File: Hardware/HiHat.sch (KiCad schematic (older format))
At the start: 34 parts, among them J1 CH trig in, J2 OH trig in, J3 IDC power connector, Q1 BC549, Q2 BC549, Q3 BC549, Q4 BC549

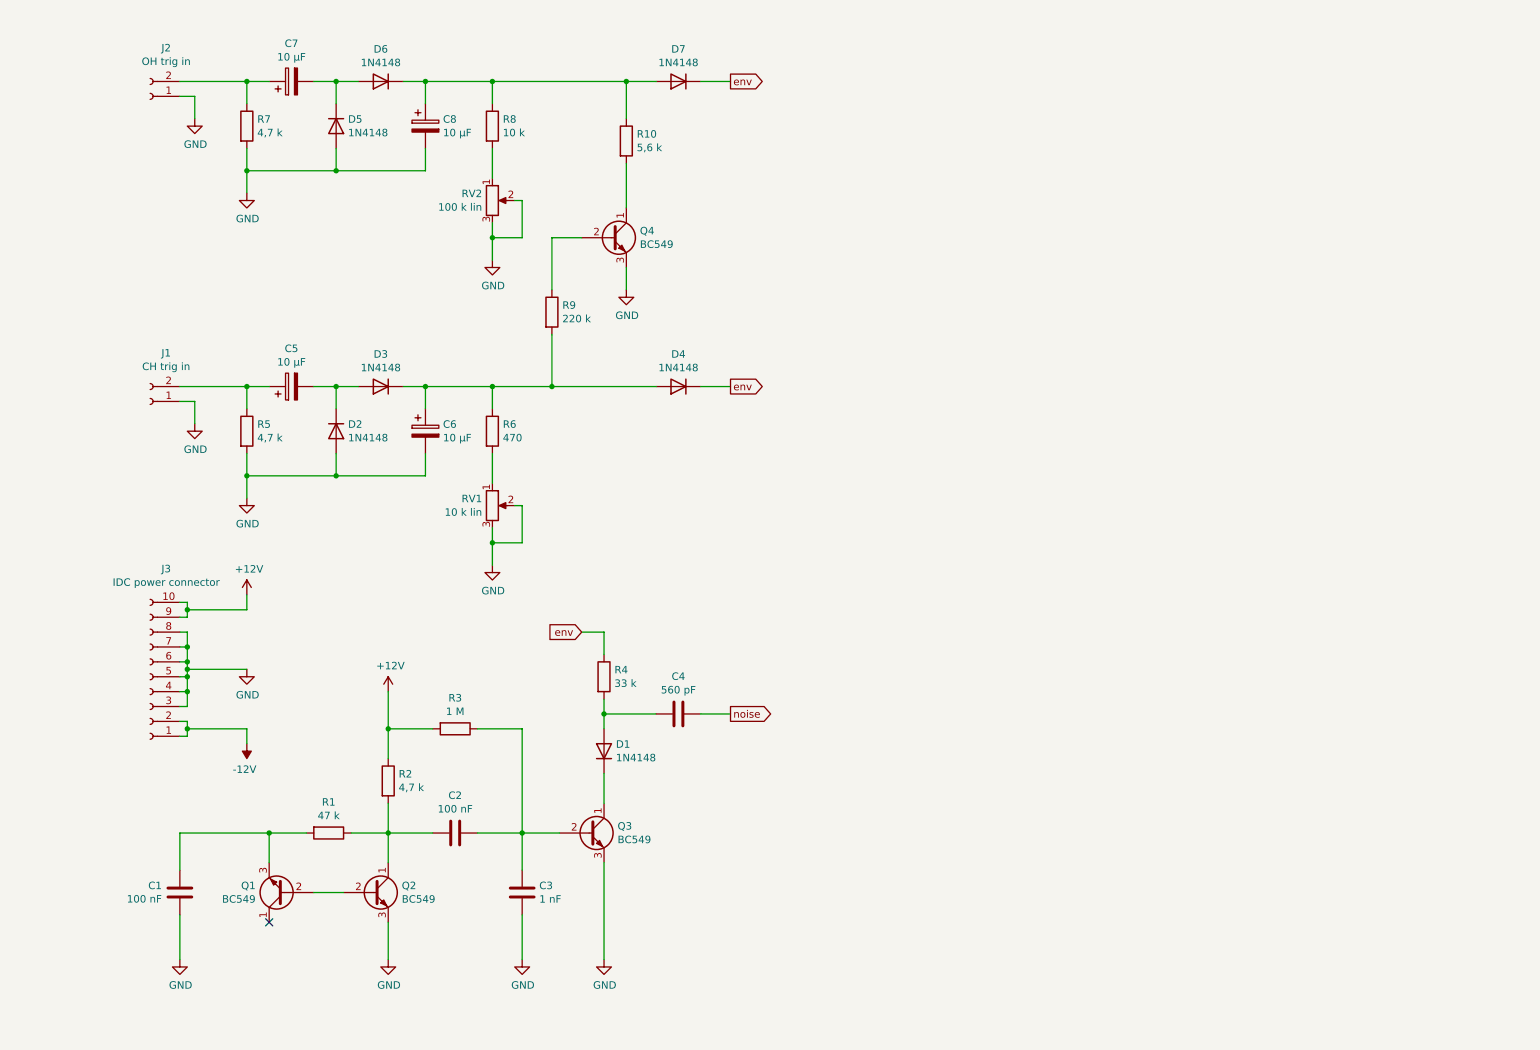
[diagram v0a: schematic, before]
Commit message: Added input conditioners and output buffer
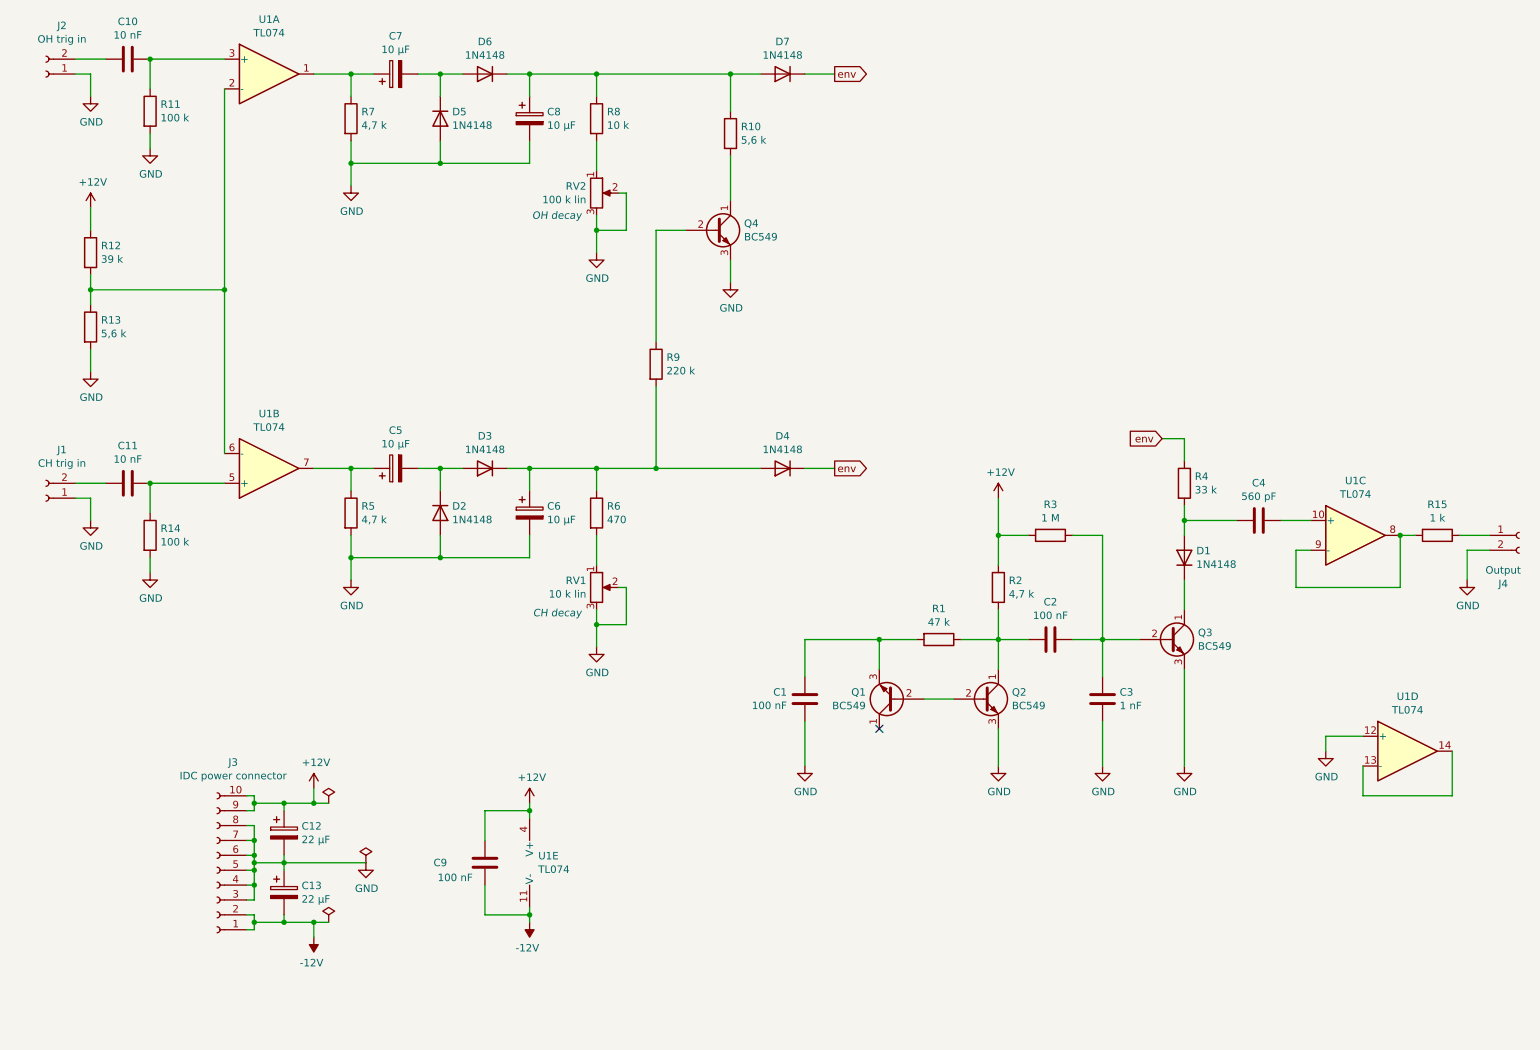
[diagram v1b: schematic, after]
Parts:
- added C10, C11: 10 nF, Capacitor_THT:C_Rect_L7.2mm_W5.5mm_P5.00mm_FKS2_FKP2_MKS2_MKP2, symbol Device:C
- added C12, C13: 22 µF, Capacitor_THT:CP_Radial_D6.3mm_P2.50mm, symbol Device:CP
- added C9: 100 nF, Capacitor_THT:C_Rect_L7.2mm_W5.5mm_P5.00mm_FKS2_FKP2_MKS2_MKP2, symbol Device:C
- added J4: Output, Connector_PinHeader_2.54mm:PinHeader_1x02_P2.54mm_Vertical, symbol Connector:Conn_01x02_Female
- added R11, R14: 100 k, Resistor_THT:R_Axial_DIN0207_L6.3mm_D2.5mm_P10.16mm_Horizontal, symbol Device:R
- added R12: 39 k, Resistor_THT:R_Axial_DIN0207_L6.3mm_D2.5mm_P10.16mm_Horizontal, symbol Device:R
- added R13: 5,6 k, Resistor_THT:R_Axial_DIN0207_L6.3mm_D2.5mm_P10.16mm_Horizontal, symbol Device:R
- added R15: 1 k, Resistor_THT:R_Axial_DIN0207_L6.3mm_D2.5mm_P10.16mm_Horizontal, symbol Device:R
- added U1: TL074, symbol Amplifier_Operational:TL074
- RV1: Label (none) -> CH decay
- RV2: Label (none) -> OH decay
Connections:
- net +12V: now also C12.1, C9.1, R12.1, U1.4 (V+)
- net -12V: now also C13.2, C9.2, U1.11 (V-)
- net GND: now also C12.2, C13.1, J4.2 (Pin_2), R11.2, R13.2, R14.2, U1.12 (+)
- net at C5.1, R5.1: now also U1.7; no longer J1.2 (Pin_2)
- net at C7.1, R7.1: now also U1.1; no longer J2.2 (Pin_2)
- net noise: no longer names the net of C4.2
- net noise: now also U1.10 (+)
- new net: C10.2, J2.2 (Pin_2)
- new net: C11.2, J1.2 (Pin_2)
- new net: R12.2, R13.1, U1.2 (-), U1.6 (-)
- new net: C10.1, R11.1, U1.3 (+)
- new net: C11.1, R14.1, U1.5 (+)
- new net: R15.2, U1.8, U1.9 (-)
- new net: U1.13 (-), U1.14
- new net: J4.1 (Pin_1), R15.1
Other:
- moved on the sheet: C1, C2, C3, C4, C5, C6, C7, C8, D1, D2, D3, D4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

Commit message: Completed sch info
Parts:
- U1: footprint (none) -> Package_DIP:DIP-14_W7.62mm_Socket_LongPads
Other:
- note added: "0.1"
- note added: "1"
- note added: "24 feb. 2021"
- note added: "Simple Hihat"
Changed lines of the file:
@@
 F 0 "U1" H 2400 1567 50  0000 C CNN
 F 1 "TL074" H 2400 1476 50  0000 C CNN
-F 2 "" H 2350 1300 50  0001 C CNN
+F 2 "Package_DIP:DIP-14_W7.62mm_Socket_LongPads" H 2350 1300 50  0001 C CNN
 F 3 "http://www.ti.com/lit/ds/symlink/tl071.pdf" H 2450 1400 50  0001 C CNN
 	1    2400 1200
@@
 F 0 "U1" H 2400 3483 50  0000 C CNN
 F 1 "TL074" H 2400 3574 50  0000 C CNN
-F 2 "" H 2350 3950 50  0001 C CNN
+F 2 "Package_DIP:DIP-14_W7.62mm_Socket_LongPads" H 2350 3950 50  0001 C CNN
 F 3 "http://www.ti.com/lit/ds/symlink/tl071.pdf" H 2450 4050 50  0001 C CNN
 	2    2400 3850
@@
 F 0 "U1" H 9700 4667 50  0000 C CNN
 F 1 "TL074" H 9700 4576 50  0000 C CNN
-F 2 "" H 9650 4400 50  0001 C CNN
+F 2 "Package_DIP:DIP-14_W7.62mm_Socket_LongPads" H 9650 4400 50  0001 C CNN
 F 3 "http://www.ti.com/lit/ds/symlink/tl071.pdf" H 9750 4500 50  0001 C CNN
 	3    9700 4300
@@
 F 0 "U1" H 10050 6117 50  0000 C CNN
 F 1 "TL074" H 10050 6026 50  0000 C CNN
-F 2 "" H 10000 5850 50  0001 C CNN
+F 2 "Package_DIP:DIP-14_W7.62mm_Socket_LongPads" H 10000 5850 50  0001 C CNN
 F 3 "http://www.ti.com/lit/ds/symlink/tl071.pdf" H 10100 5950 50  0001 C CNN
 	4    10050 5750
@@
 F 0 "U1" H 4208 6546 50  0000 L CNN
 F 1 "TL074" H 4208 6455 50  0000 L CNN
-F 2 "" H 4200 6600 50  0001 C CNN
+F 2 "Package_DIP:DIP-14_W7.62mm_Socket_LongPads" H 4200 6600 50  0001 C CNN
 F 3 "http://www.ti.com/lit/ds/symlink/tl071.pdf" H 4300 6700 50  0001 C CNN
 	5    4250 6500
@@
 Wire Wire Line
 	7000 5400 6800 5400
+Text Notes 7300 7250 0    50   ~ 0
+1
+Text Notes 7400 7250 0    50   ~ 0
+1
+Text Notes 7350 7500 0    79   ~ 0
+Simple Hihat
+Text Notes 8150 7650 0    50   ~ 0
+24 feb. 2021
+Text Notes 10600 7650 0    79   ~ 0
+0.1
 $EndSCHEMATC

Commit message: PCB routing
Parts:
- removed J1: CH trig in, Connector_PinHeader_2.54mm:PinHeader_1x02_P2.54mm_Vertical, symbol Connector:Conn_01x02_Female
- removed J2: OH trig in, Connector_PinHeader_2.54mm:PinHeader_1x02_P2.54mm_Vertical, symbol Connector:Conn_01x02_Female
- added J1: Inputs, Connector_JST:JST_EH_B3B-EH-A_1x03_P2.50mm_Vertical, symbol Connector:Conn_01x03_Female
- C4: footprint Capacitor_THT:C_Disc_D3.8mm_W2.6mm_P2.50mm -> Capacitor_THT:C_Disc_D4.3mm_W1.9mm_P5.00mm
- C9: footprint Capacitor_THT:C_Rect_L7.2mm_W5.5mm_P5.00mm_FKS2_FKP2_MKS2_MKP2 -> Capacitor_THT:C_Rect_L7.2mm_W2.5mm_P5.00mm_FKS2_FKP2_MKS2_MKP2
- D1, D2, D3, D4, D5, D6, D7: footprint Diode_THT:D_T-1_P5.08mm_Horizontal -> Diode_THT:D_DO-35_SOD27_P10.16mm_Horizontal
- J2: renamed from J4; footprint Connector_PinHeader_2.54mm:PinHeader_1x02_P2.54mm_Vertical -> Connector_JST:JST_EH_B2B-EH-A_1x02_P2.50mm_Vertical
- Q1, Q2, Q3, Q4: footprint Package_TO_SOT_THT:TO-92_Inline -> Package_TO_SOT_THT:TO-92_Inline_Wide
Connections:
- net GND: now also J1.2 (Pin_2)
- net OHtrig: now reaches C10.2
- net OHtrig: now also J1.3 (Pin_3)
- net CHtrig: now reaches C11.2
- net CHtrig: now also J1.1 (Pin_1)
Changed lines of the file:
@@
 F 0 "Q1" H 6791 5354 50  0000 L CNN
 F 1 "BC549" H 6791 5445 50  0000 L CNN
-F 2 "Package_TO_SOT_THT:TO-92_Inline" H 6800 5325 50  0001 L CIN
+F 2 "Package_TO_SOT_THT:TO-92_Inline_Wide" H 6800 5325 50  0001 L CIN
 F 3 "https://www.onsemi.com/pub/Collateral/BC550-D.pdf" H 6600 5400 50  0001 L CNN
 	1    6600 5400
@@
 F 0 "Q2" H 7391 5446 50  0000 L CNN
 F 1 "BC549" H 7391 5355 50  0000 L CNN
-F 2 "Package_TO_SOT_THT:TO-92_Inline" H 7400 5325 50  0001 L CIN
+F 2 "Package_TO_SOT_THT:TO-92_Inline_Wide" H 7400 5325 50  0001 L CIN
 F 3 "https://www.onsemi.com/pub/Collateral/BC550-D.pdf" H 7200 5400 50  0001 L CNN
 	1    7200 5400
@@
 F 0 "Q3" H 8641 5046 50  0000 L CNN
 F 1 "BC549" H 8641 4955 50  0000 L CNN
-F 2 "Package_TO_SOT_THT:TO-92_Inline" H 8650 4925 50  0001 L CIN
+F 2 "Package_TO_SOT_THT:TO-92_Inline_Wide" H 8650 4925 50  0001 L CIN
 F 3 "https://www.onsemi.com/pub/Collateral/BC550-D.pdf" H 8450 5000 50  0001 L CNN
 	1    8450 5000
@@
 F 0 "D1" V 8596 4370 50  0000 R CNN
 F 1 "1N4148" V 8505 4370 50  0000 R CNN
-F 2 "Diode_THT:D_T-1_P5.08mm_Horizontal" H 8550 4450 50  0001 C CNN
+F 2 "Diode_THT:D_DO-35_SOD27_P10.16mm_Horizontal" H 8550 4450 50  0001 C CNN
 F 3 "~" H 8550 4450 50  0001 C CNN
 	1    8550 4450
@@
 F 0 "C4" V 9302 4200 50  0000 C CNN
 F 1 "560 pF" V 9211 4200 50  0000 C CNN
-F 2 "Capacitor_THT:C_Disc_D3.8mm_W2.6mm_P2.50mm" H 9088 4050 50  0001 C CNN
+F 2 "Capacitor_THT:C_Disc_D4.3mm_W1.9mm_P5.00mm" H 9088 4050 50  0001 C CNN
 F 3 "~" H 9050 4200 50  0001 C CNN
 	1    9050 4200
@@
 F 0 "D2" V 3504 4230 50  0000 L CNN
 F 1 "1N4148" V 3595 4230 50  0000 L CNN
-F 2 "Diode_THT:D_T-1_P5.08mm_Horizontal" H 3550 4150 50  0001 C CNN
+F 2 "Diode_THT:D_DO-35_SOD27_P10.16mm_Horizontal" H 3550 4150 50  0001 C CNN
 F 3 "~" H 3550 4150 50  0001 C CNN
 	1    3550 4150
@@
 F 0 "D3" H 3850 3633 50  0000 C CNN
 F 1 "1N4148" H 3850 3724 50  0000 C CNN
-F 2 "Diode_THT:D_T-1_P5.08mm_Horizontal" H 3850 3850 50  0001 C CNN
+F 2 "Diode_THT:D_DO-35_SOD27_P10.16mm_Horizontal" H 3850 3850 50  0001 C CNN
 F 3 "~" H 3850 3850 50  0001 C CNN
 	1    3850 3850
@@
 F 0 "D4" H 5850 3633 50  0000 C CNN
 F 1 "1N4148" H 5850 3724 50  0000 C CNN
-F 2 "Diode_THT:D_T-1_P5.08mm_Horizontal" H 5850 3850 50  0001 C CNN
+F 2 "Diode_THT:D_DO-35_SOD27_P10.16mm_Horizontal" H 5850 3850 50  0001 C CNN
 F 3 "~" H 5850 3850 50  0001 C CNN
 	1    5850 3850
@@
 F 0 "D5" V 3504 1580 50  0000 L CNN
 F 1 "1N4148" V 3595 1580 50  0000 L CNN
-F 2 "Diode_THT:D_T-1_P5.08mm_Horizontal" H 3550 1500 50  0001 C CNN
+F 2 "Diode_THT:D_DO-35_SOD27_P10.16mm_Horizontal" H 3550 1500 50  0001 C CNN
 F 3 "~" H 3550 1500 50  0001 C CNN
 	1    3550 1500
@@
 F 0 "D6" H 3850 983 50  0000 C CNN
 F 1 "1N4148" H 3850 1074 50  0000 C CNN
-F 2 "Diode_THT:D_T-1_P5.08mm_Horizontal" H 3850 1200 50  0001 C CNN
+F 2 "Diode_THT:D_DO-35_SOD27_P10.16mm_Horizontal" H 3850 1200 50  0001 C CNN
 F 3 "~" H 3850 1200 50  0001 C CNN
 	1    3850 1200
@@
 F 0 "D7" H 5850 983 50  0000 C CNN
 F 1 "1N4148" H 5850 1074 50  0000 C CNN
-F 2 "Diode_THT:D_T-1_P5.08mm_Horizontal" H 5850 1200 50  0001 C CNN
+F 2 "Diode_THT:D_DO-35_SOD27_P10.16mm_Horizontal" H 5850 1200 50  0001 C CNN
 F 3 "~" H 5850 1200 50  0001 C CNN
 	1    5850 1200
@@
 F 0 "Q4" H 5591 2296 50  0000 L CNN
 F 1 "BC549" H 5591 2205 50  0000 L CNN
-F 2 "Package_TO_SOT_THT:TO-92_Inline" H 5600 2175 50  0001 L CIN
+F 2 "Package_TO_SOT_THT:TO-92_Inline_Wide" H 5600 2175 50  0001 L CIN
 F 3 "https://www.onsemi.com/pub/Collateral/BC550-D.pdf" H 5400 2250 50  0001 L CNN
 	1    5400 2250
@@
 	5500 2600 5500 2450
 $Comp
-L Connector:Conn_01x02_Female J1
-U 1 1 5FF08804
-P 900 4050
-F 0 "J1" H 792 3725 50  0000 C CNN
-F 1 "CH trig in" H 792 3816 50  0000 C CNN
-F 2 "Connector_PinHeader_2.54mm:PinHeader_1x02_P2.54mm_Vertical" H 900 4050 50  0001 C CNN
-F 3 "~" H 900 4050 50  0001 C CNN
-	1    900  4050
-	-1   0    0    1
-$EndComp
-$Comp
 L power:GND #PWR0111
 U 1 1 5FF09E17
-P 1200 1350
-F 0 "#PWR0111" H 1200 1100 50  0001 C CNN
-F 1 "GND" H 1205 1177 50  0000 C CNN
-F 2 "" H 1200 1350 50  0001 C CNN
-F 3 "" H 1200 1350 50  0001 C CNN
-	1    1200 1350
-	1    0    0    -1
-$EndComp
-$Comp
-L power:GND #PWR0112
-U 1 1 5FF0A5F7
-P 1200 4200
-F 0 "#PWR0112" H 1200 3950 50  0001 C CNN
-F 1 "GND" H 1205 4027 50  0000 C CNN
-F 2 "" H 1200 4200 50  0001 C CNN
-F 3 "" H 1200 4200 50  0001 C CNN
-	1    1200 4200
-	1    0    0    -1
-$EndComp
-Wire Wire Line
-	1200 4200 1200 4050
-Wire Wire Line
-	1200 4050 1100 4050
+P 8400 2300
+F 0 "#PWR0111" H 8400 2050 50  0001 C CNN
+F 1 "GND" H 8405 2127 50  0000 C CNN
+F 2 "" H 8400 2300 50  0001 C CNN
+F 3 "" H 8400 2300 50  0001 C CNN
+	1    8400 2300
+	1    0    0    -1
+$EndComp
 Wire Wire Line
 	9200 4200 9400 4200
@@
 	1    0    0    -1
 $EndComp
-$Comp
-L Connector:Conn_01x02_Female J2
-U 1 1 5FF05966
-P 900 1200
-F 0 "J2" H 792 875 50  0000 C CNN
-F 1 "OH trig in" H 792 966 50  0000 C CNN
-F 2 "Connector_PinHeader_2.54mm:PinHeader_1x02_P2.54mm_Vertical" H 900 1200 50  0001 C CNN
-F 3 "~" H 900 1200 50  0001 C CNN
-	1    900  1200
-	-1   0    0    1
-$EndComp
-Wire Wire Line
-	1200 1350 1200 1200
-Wire Wire Line
-	1200 1200 1100 1200
 Wire Wire Line
 	2700 1200 2950 1200
@@
 	10000 4650 10000 4300
 $Comp
-L Connector:Conn_01x02_Female J4
+L Connector:Conn_01x02_Female J2
 U 1 1 604249FC
 P 10800 4300
-F 0 "J4" H 10692 3975 50  0000 C CNN
+F 0 "J2" H 10692 3975 50  0000 C CNN
 F 1 "Output" H 10692 4066 50  0000 C CNN
-F 2 "Connector_PinHeader_2.54mm:PinHeader_1x02_P2.54mm_Vertical" H 10800 4300 50  0001 C CNN
+F 2 "Connector_JST:JST_EH_B2B-EH-A_1x02_P2.50mm_Vertical" H 10800 4300 50  0001 C CNN
 F 3 "~" H 10800 4300 50  0001 C CNN
 	1    10800 4300
@@
 F 0 "C9" H 3550 6500 50  0000 C CNN
 F 1 "100 nF" H 3650 6400 50  0000 C CNN
-F 2 "Capacitor_THT:C_Rect_L7.2mm_W5.5mm_P5.00mm_FKS2_FKP2_MKS2_MKP2" H 3888 6350 50  0001 C CNN
+F 2 "Capacitor_THT:C_Rect_L7.2mm_W2.5mm_P5.00mm_FKS2_FKP2_MKS2_MKP2" H 3888 6350 50  0001 C CNN
 F 3 "~" H 3850 6500 50  0001 C CNN
 	1    3850 6500
@@
 Text Notes 10600 7650 0    79   ~ 0
 0.1
+$Comp
+L Connector:Conn_01x03_Female J1
+U 1 1 6044EE8E
+P 7550 2000
+F 0 "J1" H 7442 1675 50  0000 C CNN
+F 1 "Inputs" H 7442 1766 50  0000 C CNN
+F 2 "Connector_JST:JST_EH_B3B-EH-A_1x03_P2.50mm_Vertical" H 7550 2000 50  0001 C CNN
+F 3 "~" H 7550 2000 50  0001 C CNN
+	1    7550 2000
+	-1   0    0    1
+$EndComp
+Text GLabel 7950 1900 2    50   Output ~ 0
+OHtrig
+Text GLabel 7950 2100 2    50   Output ~ 0
+CHtrig
+Wire Wire Line
+	7750 2100 7950 2100
+Wire Wire Line
+	7750 1900 7950 1900
+Wire Wire Line
+	7750 2000 8400 2000
+Wire Wire Line
+	8400 2000 8400 2300
+Text GLabel 1100 1100 0    50   Input ~ 0
+OHtrig
+Text GLabel 1100 3950 0    50   Input ~ 0
+CHtrig
 $EndSCHEMATC
